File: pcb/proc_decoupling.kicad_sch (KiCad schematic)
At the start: 24 parts

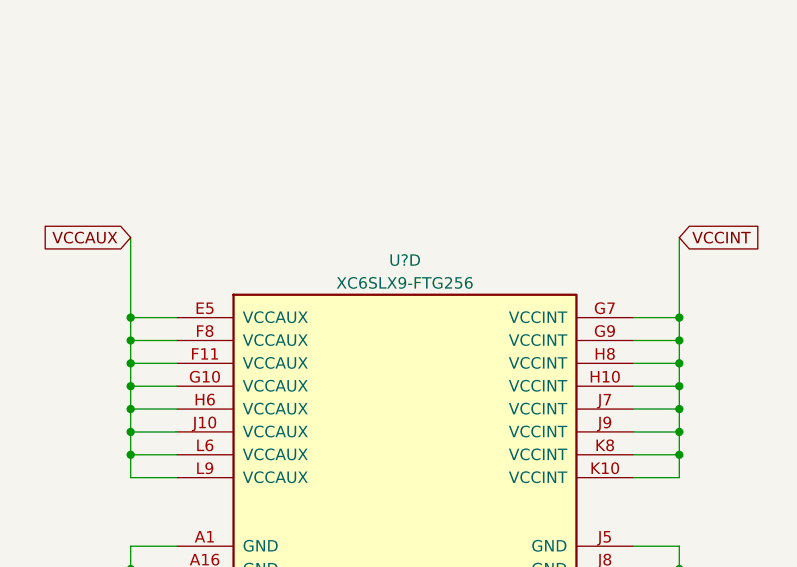
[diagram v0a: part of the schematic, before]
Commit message: add the din connector
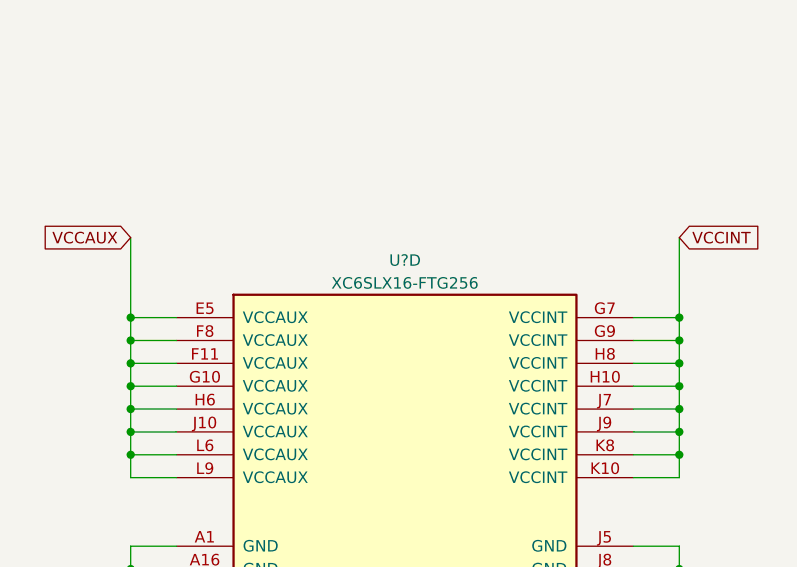
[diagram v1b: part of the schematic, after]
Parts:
- removed U?: XC6SLX9-FTG256, symbol FPGA_Xilinx_Spartan6:XC6SLX9-FTG256
- added U?: XC6SLX16-FTG256, symbol FPGA_Xilinx_Spartan6:XC6SLX16-FTG256
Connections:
- net +1V2: now also U?.G7 (VCCINT), U?.G9 (VCCINT), U?.H10 (VCCINT), U?.H8 (VCCINT), U?.J7 (VCCINT), U?.J9 (VCCINT), U?.K10 (VCCINT), U?.K8 (VCCINT)
- net +3V3: now also U?.E5 (VCCAUX), U?.F11 (VCCAUX), U?.F8 (VCCAUX), U?.G10 (VCCAUX), U?.H6 (VCCAUX), U?.J10 (VCCAUX), U?.L6 (VCCAUX), U?.L9 (VCCAUX)
- net GND: now also U?.A1 (GND), U?.A16 (GND), U?.B11 (GND), U?.B7 (GND), U?.D13 (GND), U?.D4 (GND), U?.E9 (GND), U?.G15 (GND), U?.G2 (GND), U?.G8 (GND), U?.H12 (GND), U?.H7 (GND), U?.H9 (GND), U?.J5 (GND), U?.J8 (GND), U?.K7 (GND), U?.K9 (GND), U?.L15 (GND), U?.L2 (GND), U?.M8 (GND), U?.N13 (GND), U?.P3 (GND), U?.R10 (GND), U?.R6 (GND), U?.T1 (GND), U?.T16 (GND)
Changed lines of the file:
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@@
     (pin "2")
   )
-  (symbol (lib_id "FPGA_Xilinx_Spartan6:XC6SLX9-FTG256") (at 165.1 119.38 0) (unit 4)
+  (symbol (lib_id "FPGA_Xilinx_Spartan6:XC6SLX16-FTG256") (at 165.1 119.38 0) (unit 4)
     (in_bom yes) (on_board yes) (fields_autoplaced)
     (property "Reference" "U?" (id 0) (at 165.1 85.09 0))
-    (property "Value" "XC6SLX9-FTG256" (id 1) (at 165.1 87.63 0))
+    (property "Value" "XC6SLX16-FTG256" (id 1) (at 165.1 87.63 0))
     (property "Footprint" "" (id 2) (at 165.1 119.38 0)
       (effects (font (size 1.27 1.27)) hide)

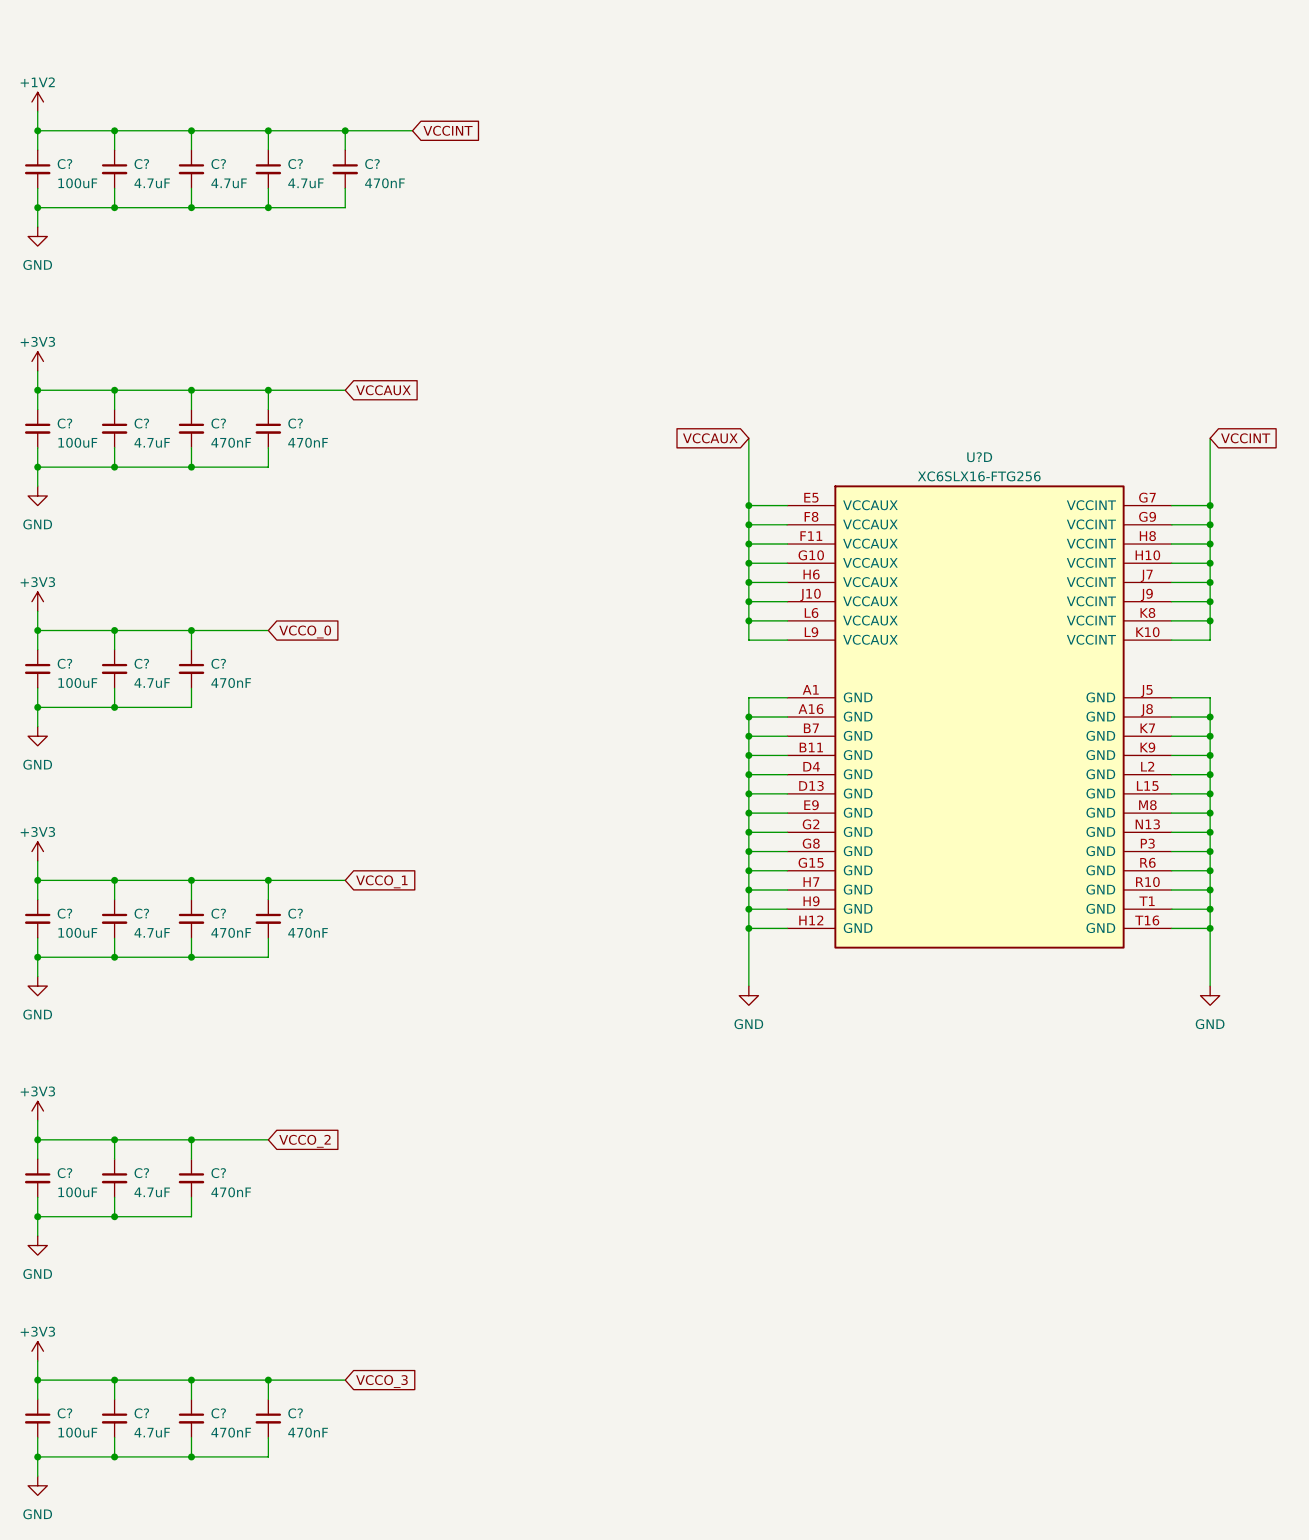
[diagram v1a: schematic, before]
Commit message: start associating footprints
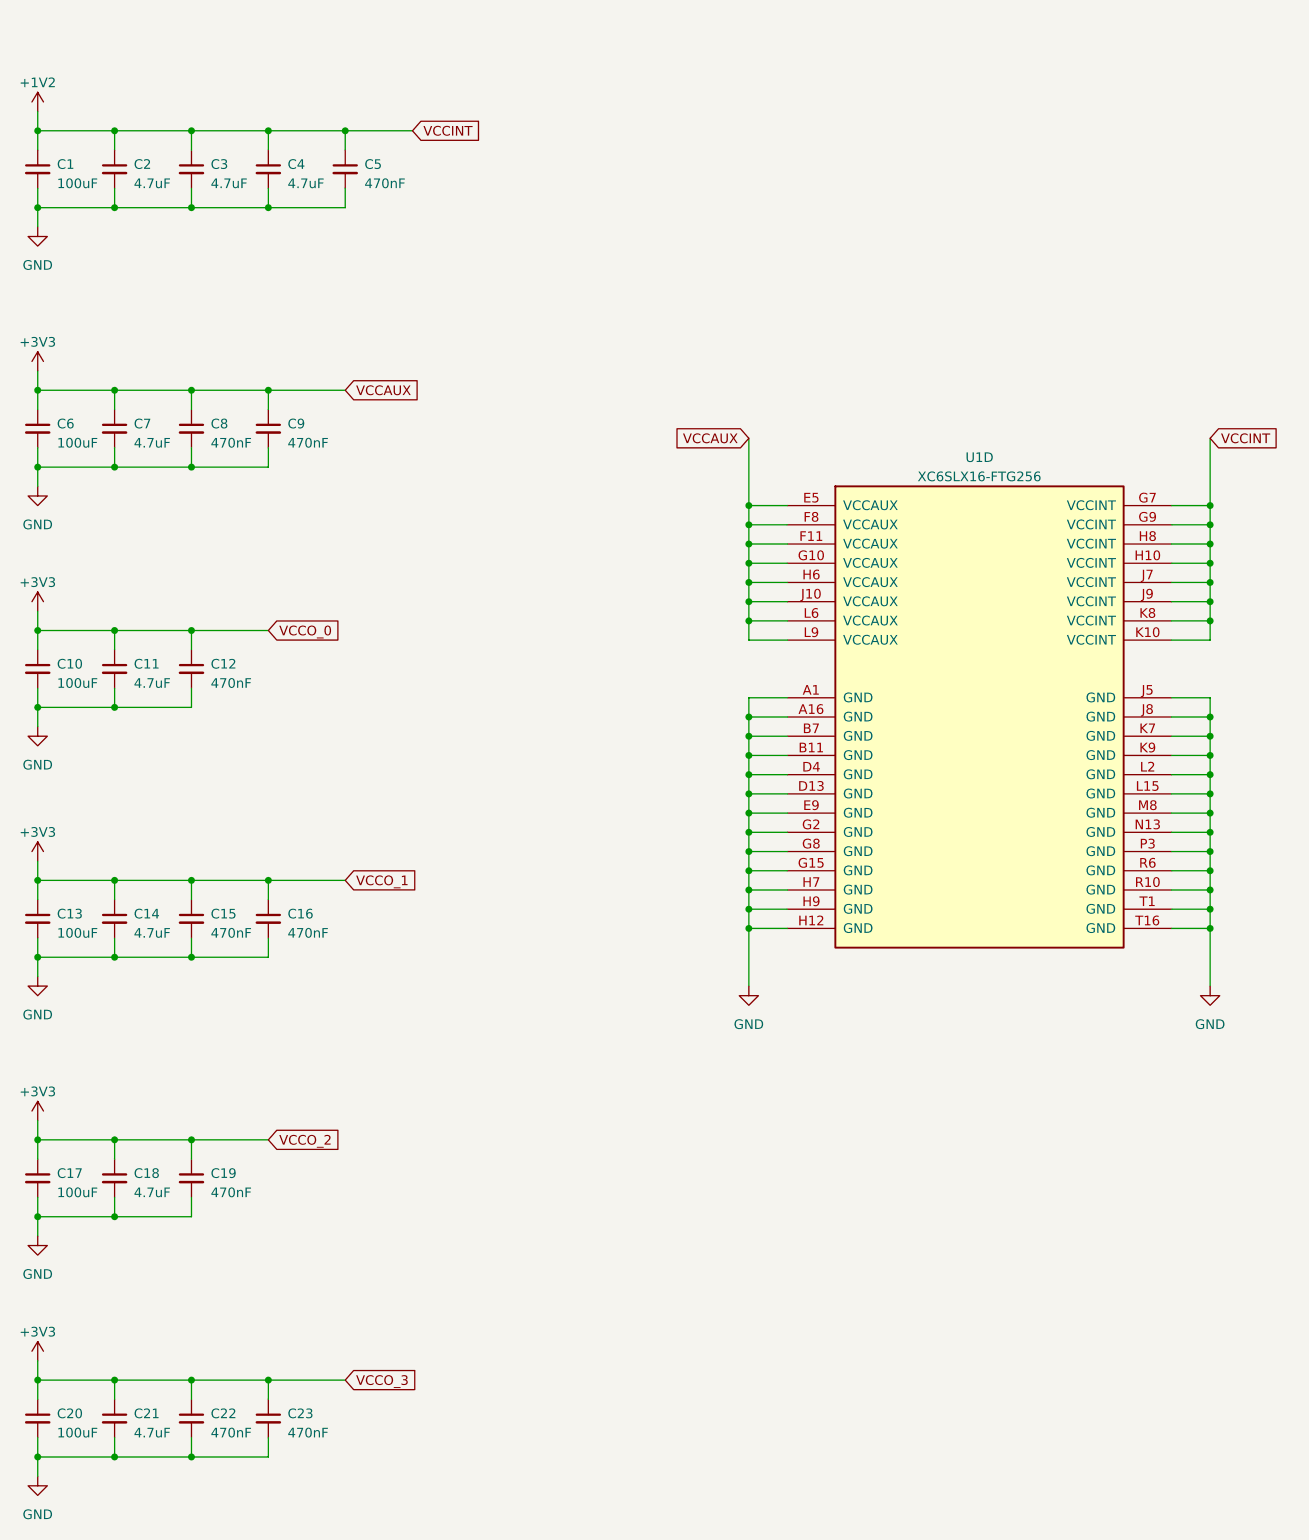
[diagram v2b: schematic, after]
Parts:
- C1, C10, C13, C17, C20, C6: renamed from C?; footprint (none) -> Capacitor_SMD:C_1210_3225Metric
- C11, C14, C18, C2, C21, C3, C4, C7: renamed from C?; footprint (none) -> Capacitor_SMD:C_0805_2012Metric
- C12, C15, C16, C19, C22, C23, C5, C8, C9: renamed from C?; footprint (none) -> Capacitor_SMD:C_0402_1005Metric
- gave numbers to parts that had none: 1

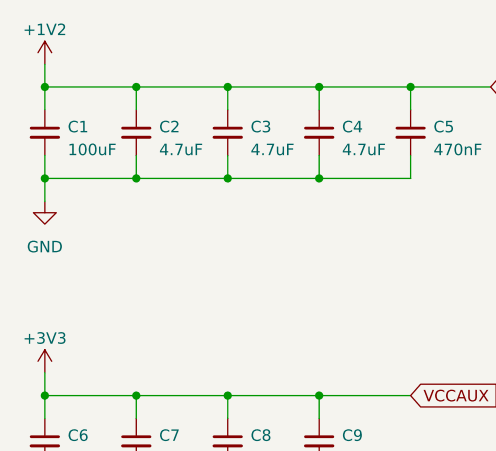
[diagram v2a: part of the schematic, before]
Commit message: add tps541620 footprint
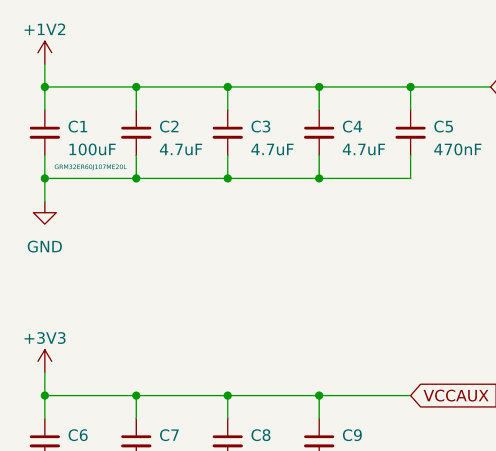
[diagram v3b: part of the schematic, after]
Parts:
- C1: Ref (none) -> GRM32ER60J107ME20L
- U1: footprint (none) -> Package_BGA:Xilinx_FTG256
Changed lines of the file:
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@@
   )
   (symbol (lib_id "Device:C_Small") (at 40.64 46.99 0) (unit 1)
-    (in_bom yes) (on_board yes) (fields_autoplaced)
+    (in_bom yes) (on_board yes)
     (property "Reference" "C1" (id 0) (at 43.18 46.3549 0)
       (effects (font (size 1.27 1.27)) (justify left))
@@
       (effects (font (size 1.27 1.27)) hide)
     )
+    (property "Ref" "GRM32ER60J107ME20L" (id 4) (at 45.72 50.8 0)
+      (effects (font (size 0.5 0.5)))
+    )
     (pin "1")
     (pin "2")
   )
   (symbol (lib_id "Device:C_Small") (at 40.64 81.28 0) (unit 1)
-    (in_bom yes) (on_board yes) (fields_autoplaced)
+    (in_bom yes) (on_board yes)
     (property "Reference" "C6" (id 0) (at 43.18 80.6449 0)
       (effects (font (size 1.27 1.27)) (justify left))
@@
   )
   (symbol (lib_id "Device:C_Small") (at 40.64 113.03 0) (unit 1)
-    (in_bom yes) (on_board yes) (fields_autoplaced)
+    (in_bom yes) (on_board yes)
     (property "Reference" "C10" (id 0) (at 43.18 112.3949 0)
       (effects (font (size 1.27 1.27)) (justify left))
@@
   )
   (symbol (lib_id "Device:C_Small") (at 40.64 146.05 0) (unit 1)
-    (in_bom yes) (on_board yes) (fields_autoplaced)
+    (in_bom yes) (on_board yes)
     (property "Reference" "C13" (id 0) (at 43.18 145.4149 0)
       (effects (font (size 1.27 1.27)) (justify left))
@@
   )
   (symbol (lib_id "Device:C_Small") (at 40.64 180.34 0) (unit 1)
-    (in_bom yes) (on_board yes) (fields_autoplaced)
+    (in_bom yes) (on_board yes)
     (property "Reference" "C17" (id 0) (at 43.18 179.7049 0)
       (effects (font (size 1.27 1.27)) (justify left))
@@
   )
   (symbol (lib_id "Device:C_Small") (at 40.64 212.09 0) (unit 1)
-    (in_bom yes) (on_board yes) (fields_autoplaced)
+    (in_bom yes) (on_board yes)
     (property "Reference" "C20" (id 0) (at 43.18 211.4549 0)
       (effects (font (size 1.27 1.27)) (justify left))
@@
     (property "Reference" "U1" (id 0) (at 165.1 85.09 0))
     (property "Value" "XC6SLX16-FTG256" (id 1) (at 165.1 87.63 0))
-    (property "Footprint" "" (id 2) (at 165.1 119.38 0)
-      (effects (font (size 1.27 1.27)) hide)
-    )
+    (property "Footprint" "Package_BGA:Xilinx_FTG256" (id 2) (at 165.1 119.38 0)
+      (effects (font (size 1.27 1.27)) hide)
+    )

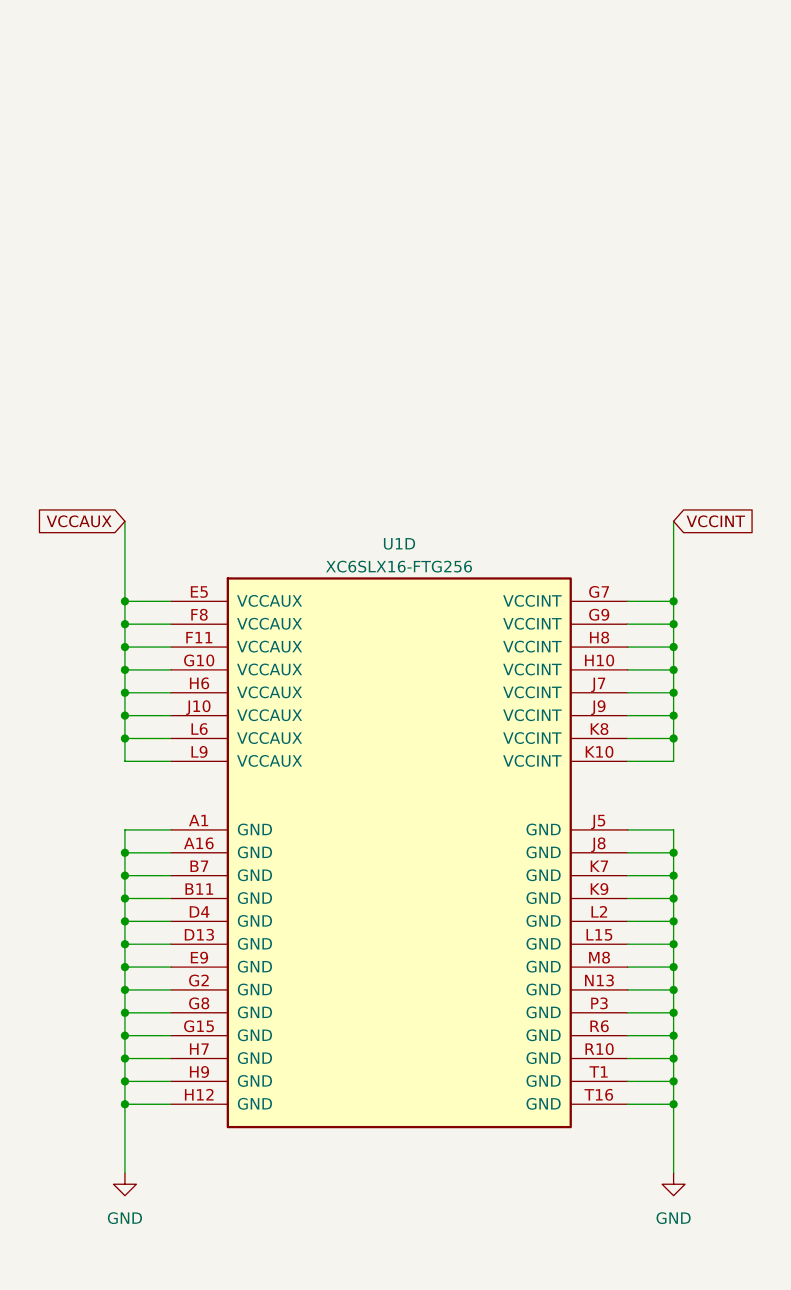
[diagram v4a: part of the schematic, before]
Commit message: change to lx9 and reduce power
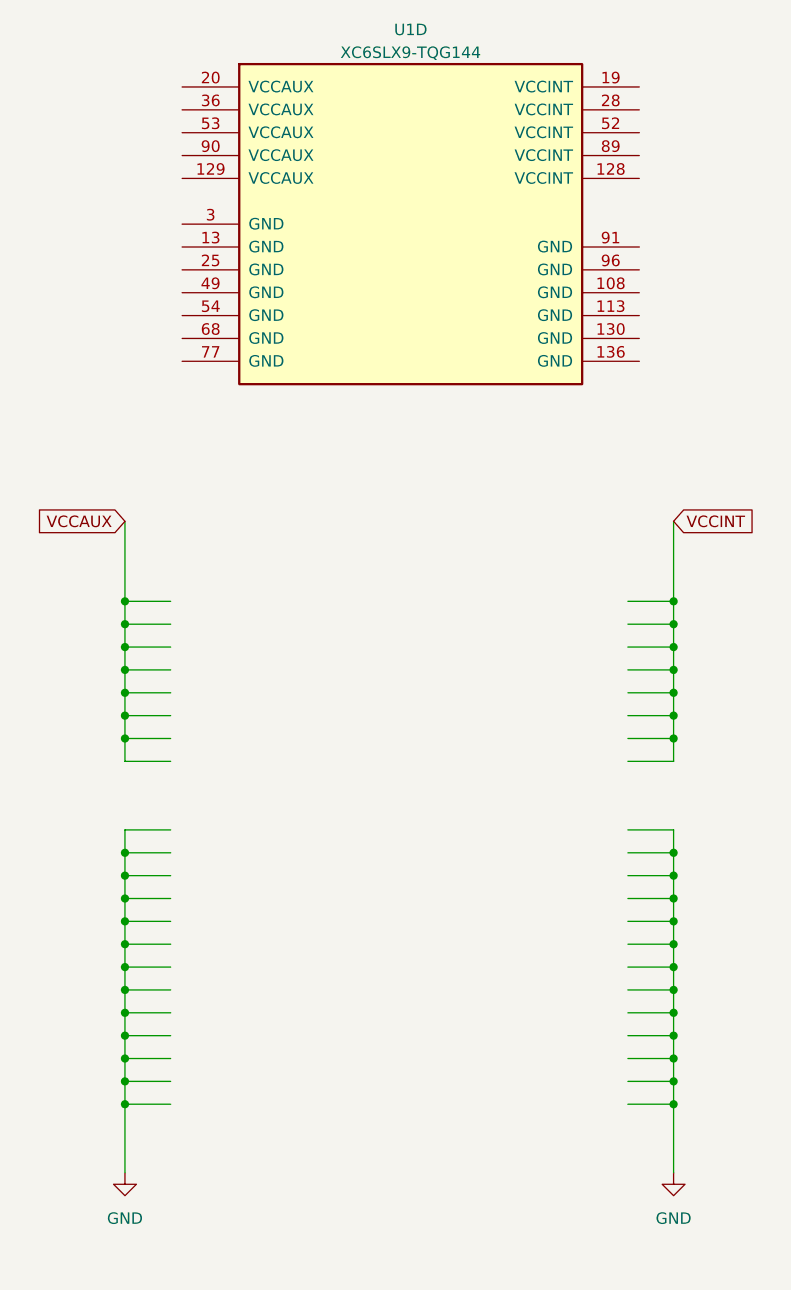
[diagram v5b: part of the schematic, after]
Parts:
- removed U1: XC6SLX16-FTG256, Package_BGA:Xilinx_FTG256, symbol FPGA_Xilinx_Spartan6:XC6SLX16-FTG256
- added U1: XC6SLX9-TQG144, Package_QFP:TQFP-144_20x20mm_P0.5mm, symbol FPGA_Xilinx_Spartan6:XC6SLX9-TQG144
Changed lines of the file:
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@@
     (pin "2")
   )
-  (symbol (lib_id "FPGA_Xilinx_Spartan6:XC6SLX16-FTG256") (at 165.1 119.38 0) (unit 4)
+  (symbol (lib_id "FPGA_Xilinx_Spartan6:XC6SLX9-TQG144") (at 166.37 49.53 0) (unit 4)
     (in_bom yes) (on_board yes) (fields_autoplaced)
-    (property "Reference" "U1" (id 0) (at 165.1 85.09 0))
-    (property "Value" "XC6SLX16-FTG256" (id 1) (at 165.1 87.63 0))
-    (property "Footprint" "Package_BGA:Xilinx_FTG256" (id 2) (at 165.1 119.38 0)
+    (property "Reference" "U1" (id 0) (at 166.37 27.94 0))
+    (property "Value" "XC6SLX9-TQG144" (id 1) (at 166.37 30.48 0))
+    (property "Footprint" "Package_QFP:TQFP-144_20x20mm_P0.5mm" (id 2) (at 166.37 49.53 0)
       (effects (font (size 1.27 1.27)) hide)
     )
-    (property "Datasheet" "" (id 3) (at 165.1 119.38 0))
-    (pin "A1")
-    (pin "A16")
-    (pin "B11")
-    (pin "B7")
-    (pin "D13")
-    (pin "D4")
-    (pin "E5")
-    (pin "E9")
-    (pin "F11")
-    (pin "F8")
-    (pin "G10")
-    (pin "G15")
-    (pin "G2")
-    (pin "G7")
-    (pin "G8")
-    (pin "G9")
-    (pin "H10")
-    (pin "H12")
-    (pin "H6")
-    (pin "H7")
-    (pin "H8")
-    (pin "H9")
-    (pin "J10")
-    (pin "J5")
-    (pin "J7")
-    (pin "J8")
-    (pin "J9")
-    (pin "K10")
-    (pin "K7")
-    (pin "K8")
-    (pin "K9")
-    (pin "L15")
-    (pin "L2")
-    (pin "L6")
-    (pin "L9")
-    (pin "M8")
-    (pin "N13")
-    (pin "P3")
-    (pin "R10")
-    (pin "R6")
-    (pin "T1")
-    (pin "T16")
+    (property "Datasheet" "" (id 3) (at 166.37 49.53 0))
+    (pin "108")
+    (pin "113")
+    (pin "128")
+    (pin "129")
+    (pin "13")
+    (pin "130")
+    (pin "136")
+    (pin "19")
+    (pin "20")
+    (pin "25")
+    (pin "28")
+    (pin "3")
+    (pin "36")
+    (pin "49")
+    (pin "52")
+    (pin "53")
+    (pin "54")
+    (pin "68")
+    (pin "77")
+    (pin "89")
+    (pin "90")
+    (pin "91")
+    (pin "96")
   )
 )
